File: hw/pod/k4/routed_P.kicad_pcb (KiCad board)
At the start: 6 copper layers, 15.5 x 12 mm, 37 parts, among them J1 TestPoint_Pad_D1.0mm, J2 TestPoint_Pad_D1.0mm, J21 CONN-SMD_BM28B0.6-30DP-2-0.35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, Q1 Nexperia_SOT1216_DFN1010B-6, Q2 Nexperia_SOT1216_DFN1010B-6, U1 QFN-48-1EP_7x7mm_P0.5mm_EP5.6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, Y1 Crystal_SMD_2012-2Pin_2.0x1.2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

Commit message: K4 B2B gap: C16/C17 (M) and C9 (P) to Samsung 0201 (0.39 max): gap side 0 fail, worst +0.05 (U3 BQ25180 / D4 0.5 max are package-fixed); D5 0.45, U3 0.5 from datasheets; M re-routed 0/0, P local edit
Co-Authored-By: Claude Opus 5.5 <noreply@anthropic.com>
Claude-Session: https://claude.ai/code/session_01Wg997D6KFs8bxoAH56jZZJ
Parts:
- C9: value C_0402_1005Metric -> C_0201_0603Metric; footprint C_0402_1005Metric -> C_0201_0603Metric

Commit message: K4 re-place/route after 9ec84ae: P and M at L 15.5, plain kicad-cli DRC 0 errors / 0 unconnected both; route_net3d GRID env; pin-contract + ECR-0020 + backlog (C9/C17 datasheet check still open)
Co-Authored-By: Claude Opus 5.5 <noreply@anthropic.com>
Claude-Session: https://claude.ai/code/session_01Wg997D6KFs8bxoAH56jZZJ
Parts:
- J2: moved to B.Cu
- moved J2 2.40 mm to (2.00, 1.20), turned to 180 degrees
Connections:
- J21 pad 1: GND -> MIC_VDD
- J21 pad 11: USB_DP -> USB_DM
- J21 pad 13: USB_DM -> USB_DP
- J21 pad 15: GND -> +3V0
- J21 pad 17: +3V0 -> GND
- J21 pad 18: +3V0 -> GND
- J21 pad 19: +3V0 -> LED_K
- J21 pad 21: GND -> MIC_DATA
- J21 pad 22: TS -> GND
- J21 pad 23: I2C_SCL -> CHG_INT
- J21 pad 25: I2C_SDA -> BTN
- J21 pad 26: CHG_INT -> GND
- J21 pad 28: VBAT_SENSE -> GND
- J21 pad 29: BTN -> TS
- J21 pad 30: LED_K -> +3V0
- J21 pad 31: (no net) -> +3V0
- J21 pad 32: (no net) -> +3V0
- J21 pad 33: (no net) -> +3V0
- J21 pad 34: (no net) -> +3V0
- J21 pad 5: GND -> VBAT_SENSE
- J21 pad 6: MIC_VDD -> GND
- J21 pad 7: MIC_DATA -> I2C_SCL
- J21 pad 9: GND -> I2C_SDA
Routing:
- net MIC_VDD: track 13.4 -> 3.55 mm, vias 2 -> 1
- net I2C_SCL: track 14.0 -> 5.23 mm, vias 2 -> 1
- net VBAT_SENSE: track 4.00 -> 11.9 mm
- net I2C_SDA: track 12.6 -> 5.32 mm, vias 2 -> 1
- net LED_K: track 12.6 -> 6.40 mm, vias 2 -> 1
- net TS: track 7.75 -> 2.32 mm
- net MIC_CLK: track 17.3 -> 12.5 mm
- net MIC_DATA: track 5.25 -> 9.98 mm, vias 1 -> 2
- net USB_DP: track 9.24 -> 4.65 mm, vias 2 -> 1
- net CHG_INT: track 14.5 -> 10.4 mm
- net USB_DM: track 8.16 -> 4.57 mm, vias 2 -> 1
- net +3V0: track 31.7 -> 34.8 mm, vias 18 -> 17
- net GB_P: track 20.0 -> 17.2 mm, vias 5 -> 6
- net BTN: track 5.03 -> 2.48 mm, vias 2 -> 1
- net OUT_A: track 10.9 -> 13.3 mm
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
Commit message: K4 routed boards: apply Value fields from values_P/M.json (no copper change; DRC 0/0 both)
Co-Authored-By: Claude Opus 5.5 <noreply@anthropic.com>
Claude-Session: https://claude.ai/code/session_01Wg997D6KFs8bxoAH56jZZJ
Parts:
- C1, C10, C2, C3, C6: value C_0201_0603Metric -> 100n
- C11, C12: value C_0201_0603Metric -> 8p2
- C14: value C_0603_1608Metric -> 22u
- C22: value C_0201_0603Metric -> 10n
- C4, C7: value C_0603_1608Metric -> 10u
- C5: value C_0402_1005Metric -> 1u
- C8: value C_0402_1005Metric -> 2u2 10V
- C9: value C_0201_0603Metric -> 2u2 10V
- J1: value TestPoint_Pad_D1.0mm -> XDCR_A
- J2: value TestPoint_Pad_D1.0mm -> XDCR_B
- J21: value CONN-SMD_BM28B0.6-30DP-2-0.35V-51 -> BM28B0.6-30DP/2-0.35V(51)
- L1: value L0806 -> 2u2
- Q1, Q2: value Nexperia_SOT1216_DFN1010B-6 -> PMCXB290UE
- R1: value R_0402_1005Metric -> 10k
- R2: value R_0201_0603Metric -> 33
- R21: value R_0402_1005Metric -> 0.1
- R22: value R_0201_0603Metric -> 1k
- R23: value R_0201_0603Metric -> 1M
- R3, R4, R5, R6: value R_0201_0603Metric -> 100k
- TP1: value TestPoint_Pad_D0.7mm -> SWDIO
- TP2: value TestPoint_Pad_D0.7mm -> SWCLK
- TP3: value TestPoint_Pad_D0.7mm -> NRST
- TP7: value TestDot_D0.5mm -> DBG_TX
- TP8: value TestDot_D0.5mm -> MDF_CCK
- TP9: value TestDot_D0.5mm -> MDF_SDI
- U1: value QFN-48-1EP_7x7mm_P0.5mm_EP5.6x5.6mm -> STM32U575CIUxQ
- Y1: value Crystal_SMD_2012-2Pin_2.0x1.2mm -> 32.768k 7pF
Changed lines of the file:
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@@
 			)
 		)
-		(property "Value" "CONN-SMD_BM28B0.6-30DP-2-0.35V-51"
+		(property "Value" "BM28B0.6-30DP/2-0.35V(51)"
 			(at 0 4.593 180)
 			(layer "F.Fab")
@@
 			)
 		)
-		(property "Value" "R_0402_1005Metric"
+		(property "Value" "0.1"
 			(at 0 1.17 0)
 			(layer "F.Fab")
@@
 			)
 		)
-		(property "Value" "R_0201_0603Metric"
+		(property "Value" "33"
 			(at 0 1.05 90)
 			(layer "F.Fab")
@@
 			)
 		)
-		(property "Value" "R_0201_0603Metric"
+		(property "Value" "100k"
 			(at 0 1.05 0)
 			(layer "F.Fab")
@@
 			)
 		)
-		(property "Value" "C_0201_0603Metric"
+		(property "Value" "10n"
 			(at 0 1.05 90)
 			(layer "F.Fab")
@@
 			)
 		)
-		(property "Value" "TestPoint_Pad_D0.7mm"
+		(property "Value" "SWDIO"
 			(at 0 0.9 0)
 			(layer "F.Fab")
@@
 			)
 		)
-		(property "Value" "TestDot_D0.5mm"
+		(property "Value" "MDF_SDI"
 			(at 0 0.9 0)
 			(layer "F.Fab")
@@
 			)
 		)
-		(property "Value" "TestPoint_Pad_D0.7mm"
+		(property "Value" "NRST"
 			(at 0 0.9 0)
 			(layer "F.Fab")
@@
 			)
 		)
-		(property "Value" "C_0201_0603Metric"
+		(property "Value" "2u2 10V"
 			(at 0 1.05 90)
 			(layer "F.Fab")
@@
 			)
 		)
-		(property "Value" "TestPoint_Pad_D0.7mm"
+		(property "Value" "SWCLK"
 			(at 0 0.9 0)
 			(layer "F.Fab")
@@
 			)
 		)
-		(property "Value" "C_0201_0603Metric"
+		(property "Value" "8p2"
 			(at 0 1.05 90)
 			(layer "F.Fab")
@@
 			)
 		)
-		(property "Value" "R_0201_0603Metric"
+		(property "Value" "100k"
 			(at 0 1.05 0)
 			(layer "F.Fab")
@@
 			)
 		)
-		(property "Value" "R_0201_0603Metric"
+		(property "Value" "1M"
 			(at 0 1.05 0)
 			(layer "F.Fab")
@@
 			)
 		)
-		(property "Value" "C_0201_0603Metric"
+		(property "Value" "100n"
 			(at 0 1.05 90)
 			(layer "F.Fab")
@@
 			)
 		)
-		(property "Value" "R_0201_0603Metric"
+		(property "Value" "1k"
 			(at 0 1.05 90)
 			(layer "F.Fab")
@@
 			)
 		)
-		(property "Value" "R_0201_0603Metric"
+		(property "Value" "100k"
 			(at 0 1.05 90)
 			(layer "F.Fab")
@@
 			)
 		)
-		(property "Value" "Nexperia_SOT1216_DFN1010B-6"
+		(property "Value" "PMCXB290UE"
 			(at 0 1.3 0)
 			(layer "F.Fab")
@@
 			)
 		)
-		(property "Value" "TestPoint_Pad_D1.0mm"
+		(property "Value" "XDCR_A"
 			(at 0 -1.55 0)
 			(layer "B.Fab")
@@
 			)
 		)
-		(property "Value" "L0806"
+		(property "Value" "2u2"
 			(at 0 -4 90)
 			(layer "B.Fab")
@@
 			)
 		)
-		(property "Value" "TestPoint_Pad_D1.0mm"
+		(property "Value" "XDCR_B"
 			(at 0 -1.55 0)
 			(layer "B.Fab")
@@
 			)
 		)
-		(property "Value" "C_0603_1608Metric"
+		(property "Value" "10u"
 			(at 0 -1.43 90)
 			(layer "B.Fab")
@@
 			)
 		)
-		(property "Value" "C_0402_1005Metric"
+		(property "Value" "2u2 10V"
 			(at 0 -1.16 90)
 			(layer "B.Fab")
@@
 			)
 		)
-		(property "Value" "C_0603_1608Metric"
+		(property "Value" "10u"
 			(at 0 -1.43 90)
 			(layer "B.Fab")
@@
 			)
 		)
-		(property "Value" "TestDot_D0.5mm"
+		(property "Value" "DBG_TX"
 			(at 0 -0.9 0)
 			(layer "B.Fab")
@@
 			)
 		)
-		(property "Value" "C_0201_0603Metric"
+		(property "Value" "100n"
 			(at 0 -1.05 90)
 			(layer "B.Fab")
@@
 			)
 		)
-		(property "Value" "C_0201_0603Metric"
+		(property "Value" "100n"
 			(at 0 -1.05 90)
 			(layer "B.Fab")
@@
 			)
 		)
-		(property "Value" "C_0201_0603Metric"
+		(property "Value" "8p2"
 			(at 0 -1.05 90)
 			(layer "B.Fab")
@@
 			)
 		)
-		(property "Value" "Crystal_SMD_2012-2Pin_2.0x1.2mm"
+		(property "Value" "32.768k 7pF"
 			(at 0 -1.8 0)
 			(layer "B.Fab")
@@
 			)
 		)
-		(property "Value" "C_0201_0603Metric"
+		(property "Value" "100n"
 			(at 0 -1.05 0)
 			(layer "B.Fab")
@@
 			)
 		)
-		(property "Value" "R_0201_0603Metric"
+		(property "Value" "100k"
 			(at 0 -1.05 90)
 			(layer "B.Fab")
@@
 			)
 		)
-		(property "Value" "Nexperia_SOT1216_DFN1010B-6"
+		(property "Value" "PMCXB290UE"
 			(at 0 -1.3 0)
 			(layer "B.Fab")
@@
 			)
 		)
-		(property "Value" "C_0603_1608Metric"
+		(property "Value" "22u"
 			(at 0 -1.43 90)
 			(layer "B.Fab")
@@
 			)
 		)
-		(property "Value" "R_0402_1005Metric"
+		(property "Value" "10k"
 			(at 0 -1.17 90)
 			(layer "B.Fab")
@@
 			)
 		)
-		(property "Value" "TestDot_D0.5mm"
+		(property "Value" "MDF_CCK"
 			(at 0 -0.9 0)
 			(layer "B.Fab")
@@
 			)
 		)
-		(property "Value" "C_0402_1005Metric"
+		(property "Value" "1u"
 			(at 0 -1.16 90)
 			(layer "B.Fab")
@@
 			)
 		)
-		(property "Value" "QFN-48-1EP_7x7mm_P0.5mm_EP5.6x5.6mm"
+		(property "Value" "STM32U575CIUxQ"
 			(at 0 -4.83 90)
 			(layer "B.Fab")
@@
 			)
 		)
-		(property "Value" "C_0201_0603Metric"
+		(property "Value" "100n"
 			(at 0 -1.05 0)
 			(layer "B.Fab")

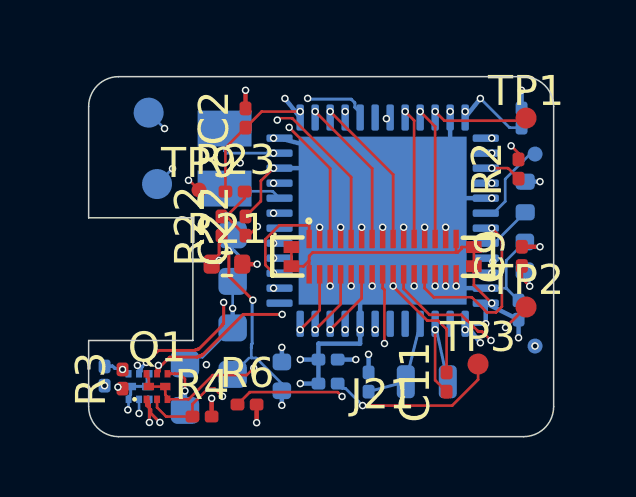
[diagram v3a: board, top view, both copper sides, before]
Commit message: K4 boards: clear all DRC warnings (refdes hidden, flagged silk removed, redundant GB_P via/stubs); release rebuilt on new hashes
Co-Authored-By: Claude Opus 5.5 <noreply@anthropic.com>
Claude-Session: https://claude.ai/code/session_01Wg997D6KFs8bxoAH56jZZJ
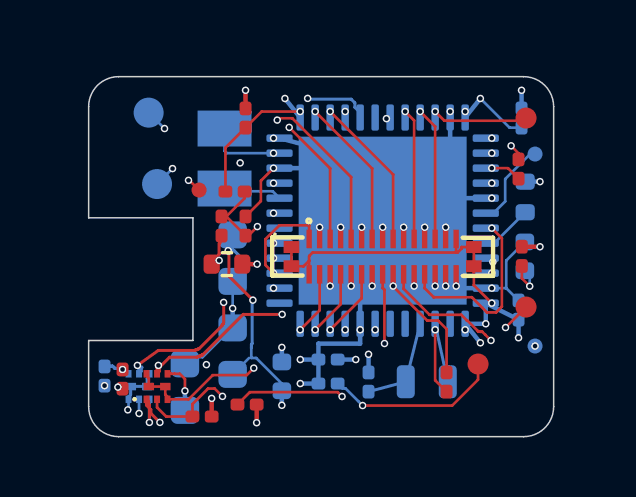
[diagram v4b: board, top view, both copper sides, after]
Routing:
- net GB_P: vias 6 -> 5
